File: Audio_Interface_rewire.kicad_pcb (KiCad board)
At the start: 2 copper layers, 115 x 67.5 mm, 62 parts, among them IC1 REG103GA-3.3_2K5, IC2 PCM2906CDB, IC3 INA849DGKT, J1 USB_B_Micro, J2 SJ-435107RS, J3 Vol. knob1 22k, J4 Vol. knob2 22k, J5 SW_PUSH_3PDT, J6 External mic. conn., Q1 J304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

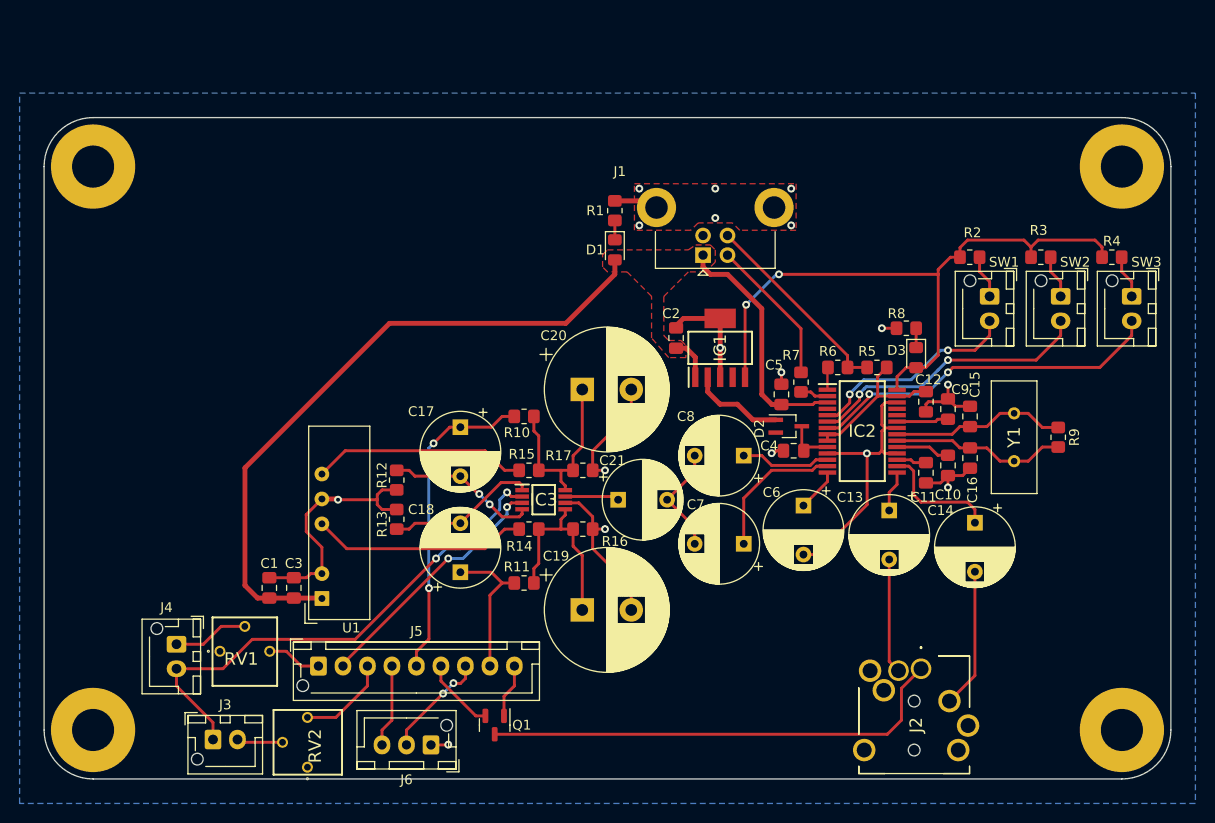
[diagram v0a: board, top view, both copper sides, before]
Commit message: Revert "Finished pcb layout for version 2.0"
This reverts commit 9c98f4441856926bdc06a9c73f1d06339f9013c3. Pushed to wrong branch
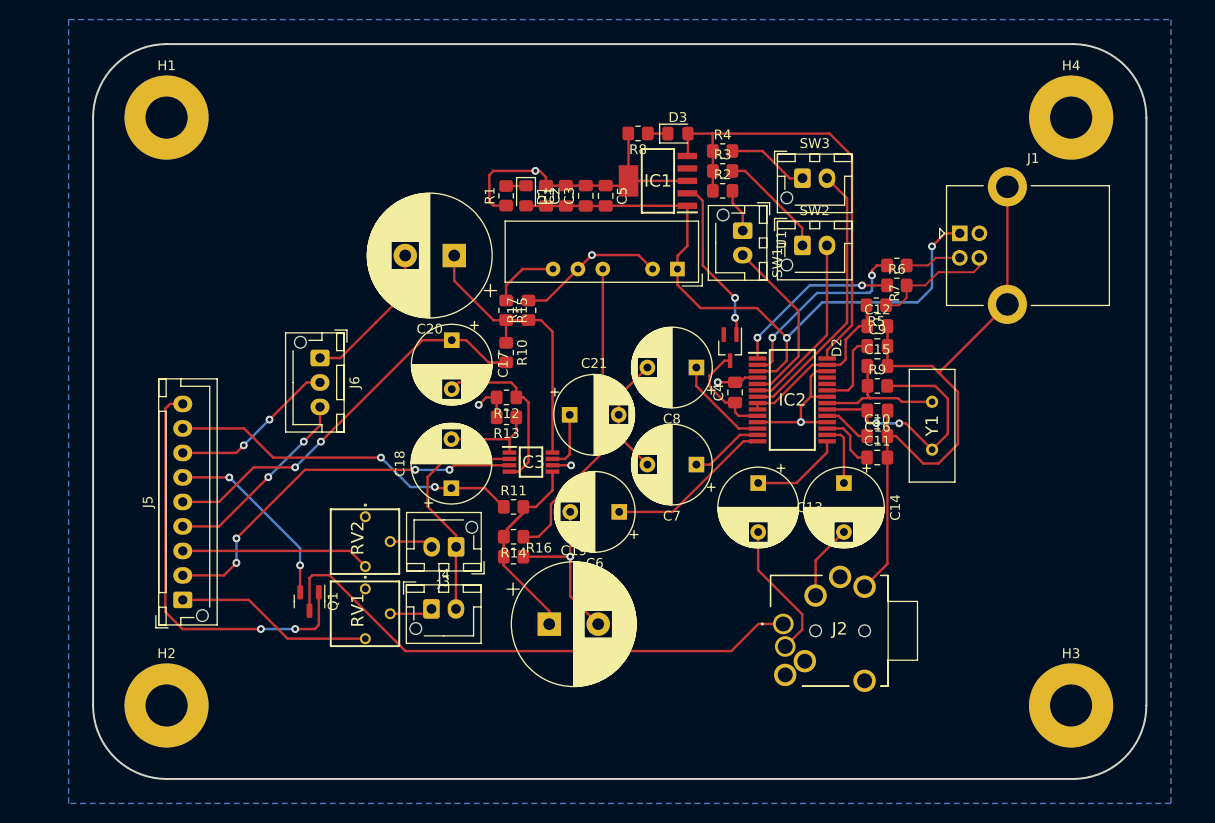
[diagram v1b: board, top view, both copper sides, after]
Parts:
- moved H1 115.8 mm to (97.5, 70.0)
- moved H2 111.9 mm to (97.5, 130.0)
- moved H4 99.9 mm to (189.8, 70.0)
- moved H3 99.8 mm to (189.8, 130.0)
- moved C1 50.2 mm to (138.2, 78.0)
- moved C3 49.9 mm to (140.3, 78.0)
- moved U1 49.5 mm to (149.6, 85.5), turned to -90 degrees
- moved R4 41.2 mm to (154.3, 73.4)
- moved J6 41.1 mm to (113.2, 94.5), turned to -90 degrees
- moved SW3 35.7 mm to (162.4, 76.2), turned to 0 degrees
- moved R8 33.8 mm to (145.6, 71.6)
- moved R3 33.6 mm to (154.3, 75.4)
- moved D3 33.4 mm to (149.7, 71.6), turned to 0 degrees
- moved J3 31.7 mm to (127.1, 113.8), turned to 180 degrees
- moved C5 27.1 mm to (142.3, 78.0)
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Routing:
- net GND: track 117.3 -> 172.3 mm, vias 17 -> 7
- net /INT_MIC_D: track 5.53 -> 42.6 mm, vias 0 -> 2
- net /RG_1: track 52.3 -> 23.8 mm, vias 2 -> 0
- net VBUS: track 97.1 -> 68.7 mm, vias 0 -> 2
- net /V_IN_D: track 14.9 -> 36.1 mm, vias 0 -> 2
- net /~{SSPND}: track 65.0 -> 47.6 mm, vias 2 -> 0
- net Net-(IC2-Pad2): track 2.88 -> 20.0 mm, vias 0 -> 2
- net Net-(IC2-Pad1): track 2.30 -> 17.6 mm, vias 0 -> 2
- net +15V: track 21.9 -> 7.02 mm
- net /hp_mic: track 5.60 -> 20.3 mm
- net /RG_2: track 25.8 -> 39.5 mm, vias 2 -> 4
- net Net-(C6-Pad1): track 4.39 -> 17.1 mm
- net /INT_MIC_S: track 7.54 -> 19.5 mm, vias 0 -> 2
- net /EXT_MIC_S: track 8.47 -> 20.2 mm, vias 0 -> 2
- net /HID1: track 29.3 -> 18.6 mm, vias 2 -> 0
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- removed copper zone on F.Cu, net GND
- removed copper zone on F.Cu, net VBUS
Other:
- board size 115 x 67.5 mm -> 107.5 x 75 mm
